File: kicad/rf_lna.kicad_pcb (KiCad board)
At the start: 4 copper layers, 100 x 100 mm, 69 parts, among them J1 Conn_01x02_Pin, J2 Conn_Coaxial_Small, J3 Conn_Coaxial_Small, J4 Conn_01x02_Pin, J5 Conn_Coaxial_Small, J6 Conn_Coaxial_Small, J7 Conn_Coaxial_Small, J8 Conn_Coaxial_Small, J9 Conn_Coaxial_Small, U1 L78L05_SOT89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

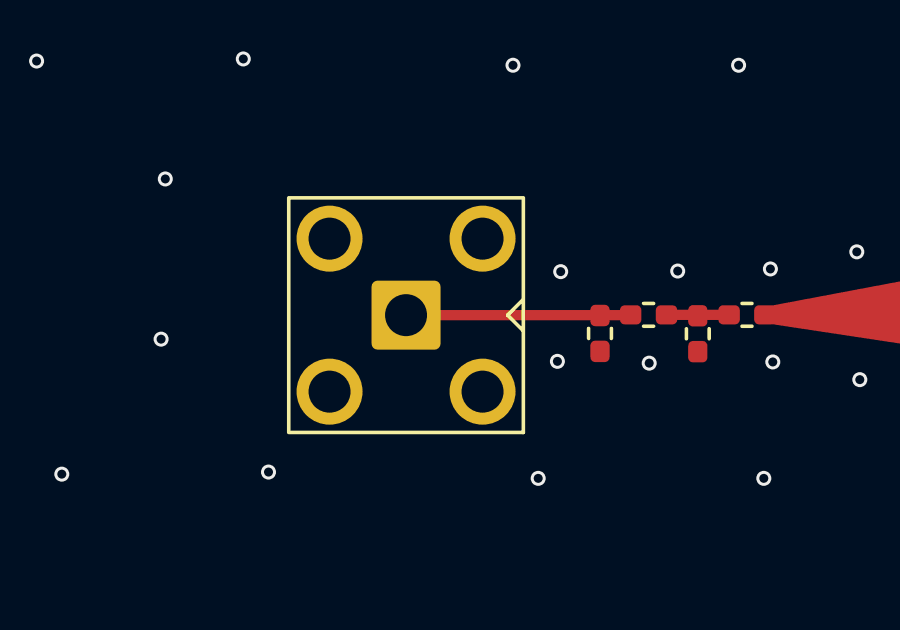
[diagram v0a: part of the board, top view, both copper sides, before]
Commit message: [kicad] Removed excess dimensioning on antenna, added extra vias around sma connector
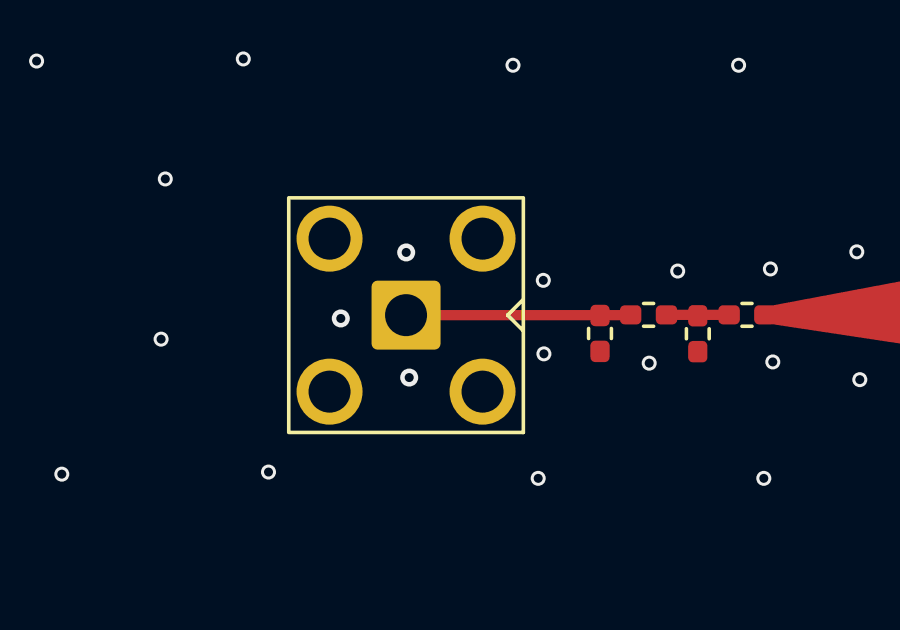
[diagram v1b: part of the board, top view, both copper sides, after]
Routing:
- net GND: vias 230 -> 233
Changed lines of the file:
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@@
 		)
 		(fp_text user "${REFERENCE}"
-			(at 0 5 360)
+			(at 0 5 0)
 			(layer "F.Fab")
 			(effects
@@
 		)
 		(fp_text user "${REFERENCE}"
-			(at 0 5 360)
+			(at 0 5 0)
 			(layer "F.Fab")
 			(effects
@@
 		(layer "F.SilkS")
 		(pts
-			(xy 134.1 147.65) (xy 143.1 147.65)
-		)
-		(height 0)
-		(gr_text "9 mm"
-			(at 138.6 146.55 0)
-			(layer "F.SilkS")
-			(effects
-				(font
-					(size 1 1)
-					(thickness 0.1)
-				)
-			)
-		)
-		(format
-			(prefix "")
-			(suffix "")
-			(units 3)
-			(units_format 1)
-			(precision 4)
-			(override_value "9")
-		)
-		(style
-			(thickness 0.1)
-			(arrow_length 1.27)
-			(text_position_mode 0)
-			(extension_height 0.58642)
-			(extension_offset 0.5) keep_text_aligned)
-	)
-	(dimension
-		(type aligned)
-		(layer "F.SilkS")
-		(pts
 			(xy 140.125 111.75) (xy 149.125 111.75)
 		)
@@
 	)
 	(via
+		(at 100.83 127.81)
+		(size 0.6)
+		(drill 0.3)
+		(layers "F.Cu" "B.Cu")
+		(free yes)
+		(net 5)
+	)
+	(via
 		(at 79.02 121.57)
 		(size 0.5)
@@
 	)
 	(via
+		(at 100.93 131.98)
+		(size 0.6)
+		(drill 0.3)
+		(layers "F.Cu" "B.Cu")
+		(free yes)
+		(net 5)
+	)
+	(via
 		(at 125.27 76.89)
 		(size 0.5)
@@
 	)
 	(via
-		(at 105.87 131.44)
+		(at 105.42 131.19)
 		(size 0.5)
 		(drill 0.3)
@@
 	)
 	(via
+		(at 98.65 130.01)
+		(size 0.6)
+		(drill 0.3)
+		(layers "F.Cu" "B.Cu")
+		(free yes)
+		(net 5)
+	)
+	(via
 		(at 126.23 73.82)
 		(size 0.5)
@@
 	)
 	(via
-		(at 105.98 128.45)
+		(at 105.4 128.74)
 		(size 0.5)
 		(drill 0.3)
